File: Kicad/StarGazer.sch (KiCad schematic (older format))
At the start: 17 parts, among them U101 STM32G070KBT6

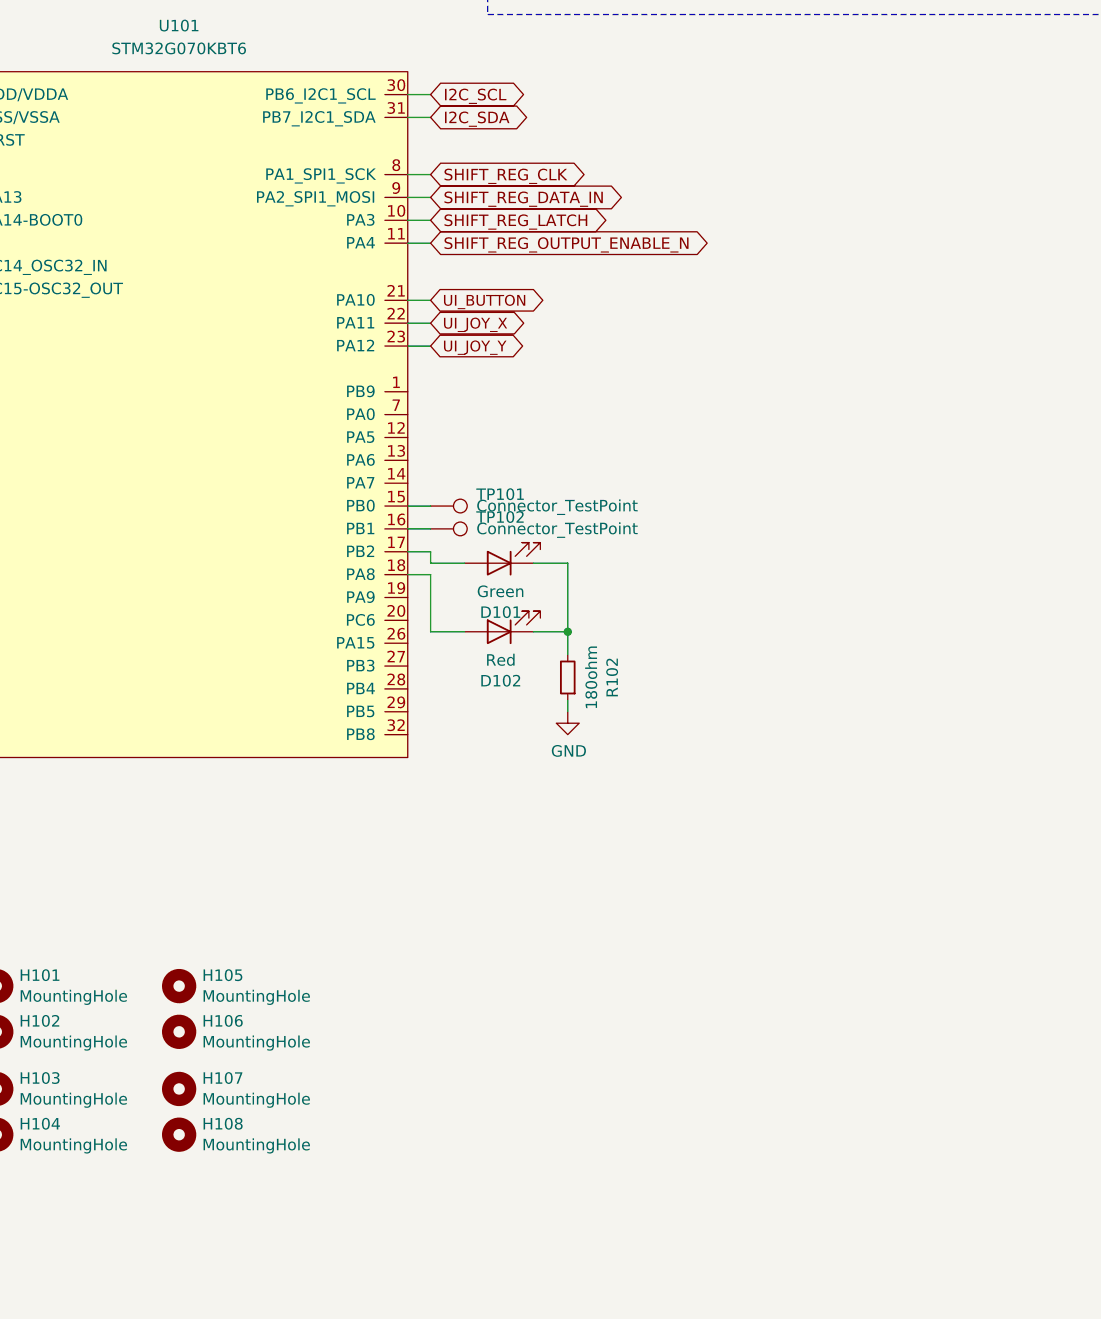
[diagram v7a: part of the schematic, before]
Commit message: Continued work on PCB.  Added back art.
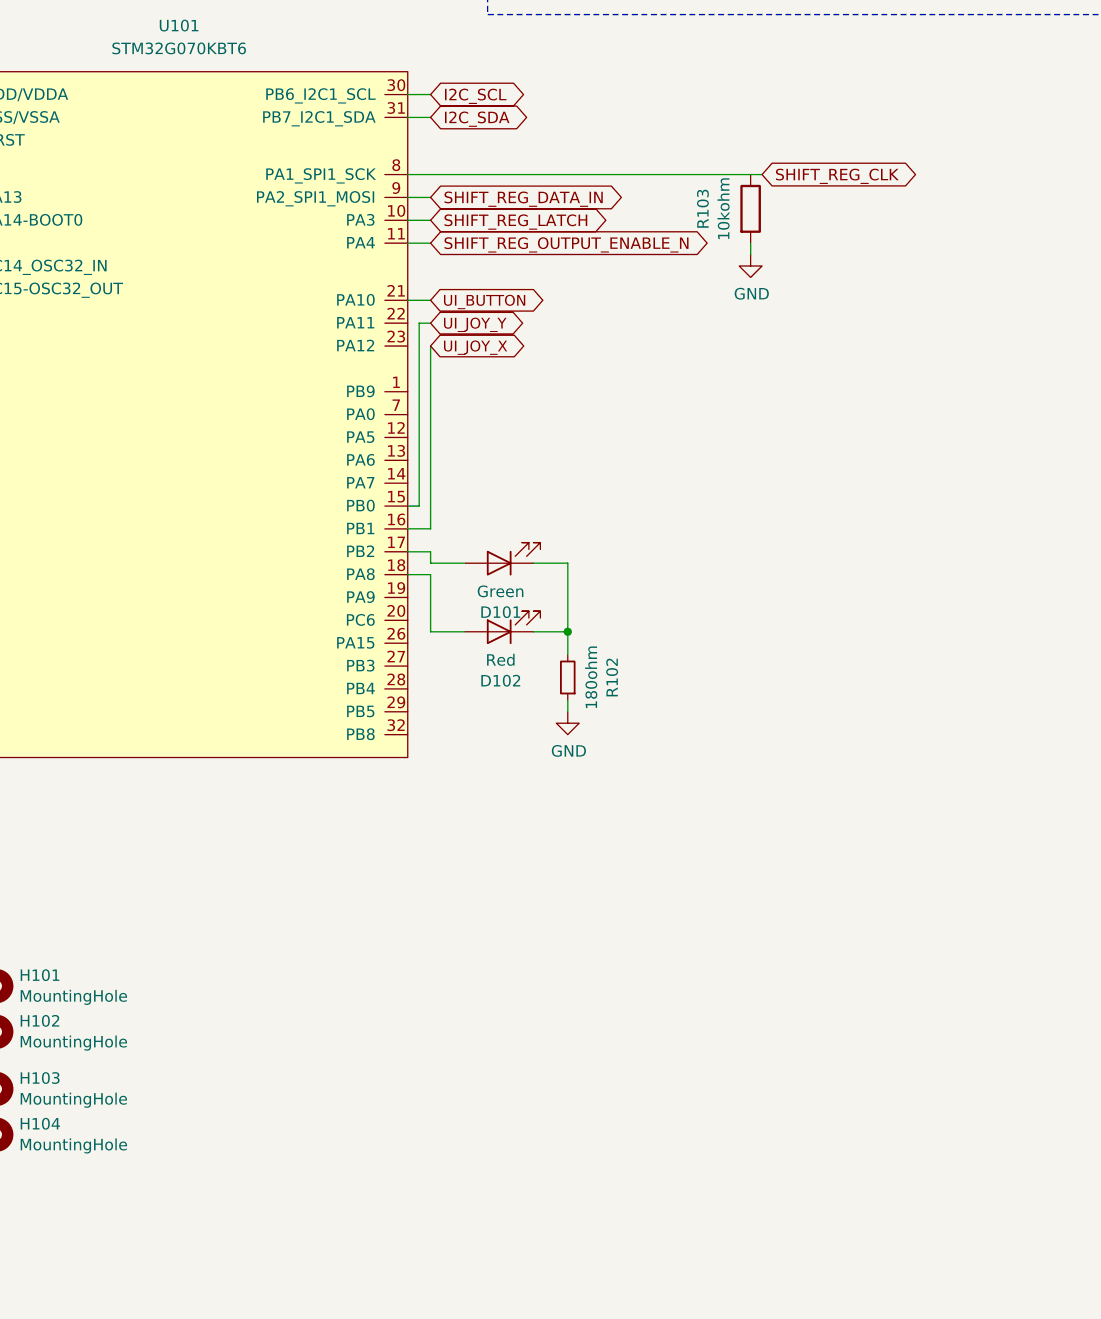
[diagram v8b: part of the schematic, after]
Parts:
- removed H105, H106, H107, H108: MountingHole, MountingHole:MountingHole_2.2mm_M2, symbol Mechanical:MountingHole
- removed TP101, TP102: Connector_TestPoint, TestPoint:TestPoint_Pad_D1.0mm, symbol StarGazer-cache:Connector_TestPoint
- added R103: 10kohm, Resistor_SMD:R_1206_3216Metric_Pad1.42x1.75mm_HandSolder, symbol Device:R
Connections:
- net GND: now also R103.2
- net UI_JOY_X: now also U101.16 (PB1); no longer U101.22 (PA11)
- net UI_JOY_Y: now also U101.15 (PB0); no longer U101.23 (PA12)
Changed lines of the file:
@@
 Text GLabel 6700 3400 2    50   BiDi ~ 0
 SHIFT_REG_LATCH
-Text GLabel 6700 3200 2    50   BiDi ~ 0
+Text GLabel 8150 3200 2    50   BiDi ~ 0
 SHIFT_REG_CLK
 Text GLabel 6700 3300 2    50   BiDi ~ 0
@@
 Text GLabel 6700 3750 2    47   BiDi ~ 0
 UI_BUTTON
+Text GLabel 6700 3950 2    47   BiDi ~ 0
+UI_JOY_X
 Text GLabel 6700 3850 2    47   BiDi ~ 0
-UI_JOY_X
-Text GLabel 6700 3950 2    47   BiDi ~ 0
 UI_JOY_Y
 $Sheet
@@
 $EndComp
 Wire Wire Line
-	6700 3950 6600 3950
-Wire Wire Line
-	6600 3850 6700 3850
-Wire Wire Line
 	6700 3750 6600 3750
-Wire Wire Line
-	6600 3200 6700 3200
 Wire Wire Line
 	6700 3300 6600 3300
@@
 Wire Notes Line
 	6950 2500 10200 2500
-$Comp
-L StarGazer-cache:Connector_TestPoint TP101
-U 1 1 5F780150
-P 6700 4650
-F 0 "TP101" V 6650 4850 50  0000 L CNN
-F 1 "Connector_TestPoint" V 6700 4850 50  0000 L CNN
-F 2 "TestPoint:TestPoint_Pad_D1.0mm" H 6900 4650 50  0001 C CNN
-F 3 "" H 6900 4650 50  0001 C CNN
-F 4 "Test point for Cortex" H 6700 4650 50  0001 C CNN "part_details"
-	1    6700 4650
-	0    1    1    0
-$EndComp
-$Comp
-L StarGazer-cache:Connector_TestPoint TP102
-U 1 1 5F783255
-P 6700 4750
-F 0 "TP102" V 6650 4950 50  0000 L CNN
-F 1 "Connector_TestPoint" V 6700 4950 50  0000 L CNN
-F 2 "TestPoint:TestPoint_Pad_D1.0mm" H 6900 4750 50  0001 C CNN
-F 3 "" H 6900 4750 50  0001 C CNN
-F 4 "Test point for Cortex" H 6700 4750 50  0001 C CNN "part_details"
-	1    6700 4750
-	0    1    1    0
-$EndComp
-Wire Wire Line
-	6600 4650 6700 4650
+Wire Wire Line
+	6600 4650 6650 4650
 Wire Wire Line
 	6600 4750 6700 4750
@@
 $EndComp
 $Comp
-L Mechanical:MountingHole H107
-U 1 1 5F61C377
-P 5600 7200
-F 0 "H107" H 5700 7246 50  0000 L CNN
-F 1 "MountingHole" H 5700 7155 50  0000 L CNN
-F 2 "MountingHole:MountingHole_2.2mm_M2" H 5600 7200 50  0001 C CNN
-F 3 "~" H 5600 7200 50  0001 C CNN
-F 4 "DO_NOT_SHOW" H 5600 7200 50  0001 C CNN "part_details"
-	1    5600 7200
-	1    0    0    -1
-$EndComp
-$Comp
-L Mechanical:MountingHole H108
-U 1 1 5F61C9F3
-P 5600 7400
-F 0 "H108" H 5700 7446 50  0000 L CNN
-F 1 "MountingHole" H 5700 7355 50  0000 L CNN
-F 2 "MountingHole:MountingHole_2.2mm_M2" H 5600 7400 50  0001 C CNN
-F 3 "~" H 5600 7400 50  0001 C CNN
-F 4 "DO_NOT_SHOW" H 5600 7400 50  0001 C CNN "part_details"
-	1    5600 7400
-	1    0    0    -1
-$EndComp
-$Comp
-L Mechanical:MountingHole H105
-U 1 1 5F61EB9F
-P 5600 6750
-F 0 "H105" H 5700 6796 50  0000 L CNN
-F 1 "MountingHole" H 5700 6705 50  0000 L CNN
-F 2 "MountingHole:MountingHole_2.2mm_M2" H 5600 6750 50  0001 C CNN
-F 3 "~" H 5600 6750 50  0001 C CNN
-F 4 "DO_NOT_SHOW" H 5600 6750 50  0001 C CNN "part_details"
-	1    5600 6750
-	1    0    0    -1
-$EndComp
-$Comp
-L Mechanical:MountingHole H106
-U 1 1 5F61EBA6
-P 5600 6950
-F 0 "H106" H 5700 6996 50  0000 L CNN
-F 1 "MountingHole" H 5700 6905 50  0000 L CNN
-F 2 "MountingHole:MountingHole_2.2mm_M2" H 5600 6950 50  0001 C CNN
-F 3 "~" H 5600 6950 50  0001 C CNN
-F 4 "DO_NOT_SHOW" H 5600 6950 50  0001 C CNN "part_details"
-	1    5600 6950
-	1    0    0    -1
-$EndComp
-$Comp
 L Mechanical:MountingHole H103
 U 1 1 5F61FCE3
@@
 Wire Wire Line
 	7300 5550 7300 5500
+Wire Wire Line
+	6650 4650 6650 3850
+Wire Wire Line
+	6650 3850 6700 3850
+Wire Wire Line
+	6700 3950 6700 4750
+Wire Wire Line
+	6600 3200 8150 3200
+Wire Wire Line
+	8100 3550 8100 3500
+$Comp
+L power:GND #PWR0104
+U 1 1 5F70674D
+P 8100 3550
+F 0 "#PWR0104" H 8100 3300 50  0001 C CNN
+F 1 "GND" H 8105 3377 50  0000 C CNN
+F 2 "" H 8100 3550 50  0001 C CNN
+F 3 "" H 8100 3550 50  0001 C CNN
+	1    8100 3550
+	1    0    0    -1
+$EndComp
+$Comp
+L Device:R R103
+U 1 1 5F706757
+P 8100 3350
+F 0 "R103" V 7893 3350 50  0000 C CNN
+F 1 "10kohm" V 7984 3350 50  0000 C CNN
+F 2 "Resistor_SMD:R_1206_3216Metric_Pad1.42x1.75mm_HandSolder" V 8030 3350 50  0001 C CNN
+F 3 "~" H 8100 3350 50  0001 C CNN
+F 4 "" H 8100 3350 50  0001 C CNN "Name"
+F 5 "" H 8100 3350 50  0001 C CNN "part_details"
+F 6 "Resistor - Pull Up" H 8100 3350 50  0001 C CNN "part_name"
+F 7 "https://www.digikey.com/product-detail/en/yageo/RC1206JR-0710KL/311-10KERCT-ND/732156" H 8100 3350 50  0001 C CNN "part_url"
+	1    8100 3350
+	1    0    0    -1
+$EndComp
 $EndSCHEMATC
